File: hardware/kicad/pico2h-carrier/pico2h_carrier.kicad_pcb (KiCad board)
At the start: 2 copper layers, 92 x 82 mm, 0 parts

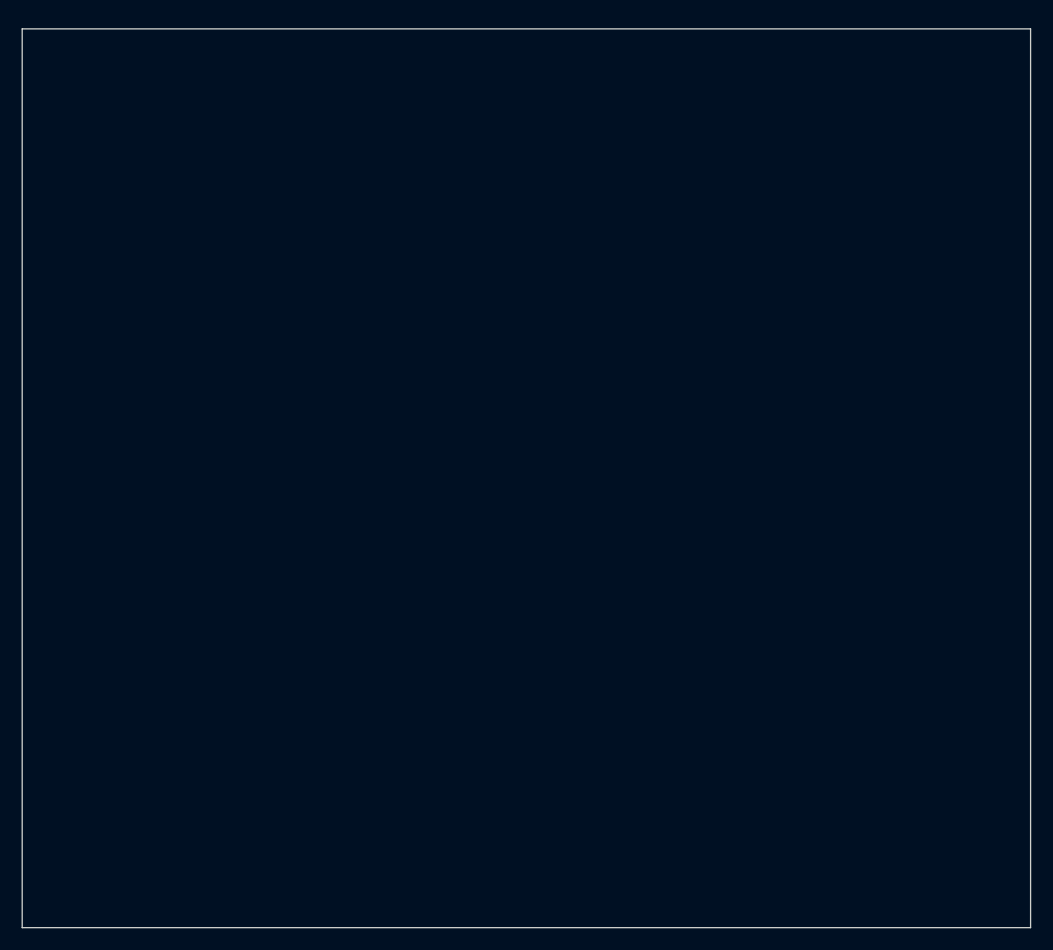
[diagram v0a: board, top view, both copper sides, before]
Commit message: feat: Pico 2 Hケースを58x38 mm基板・背面カメラのRev Cへ変更
基板を小さくし、カメラを背面へ移したうえで、印刷できる区切りの形状を残すため。
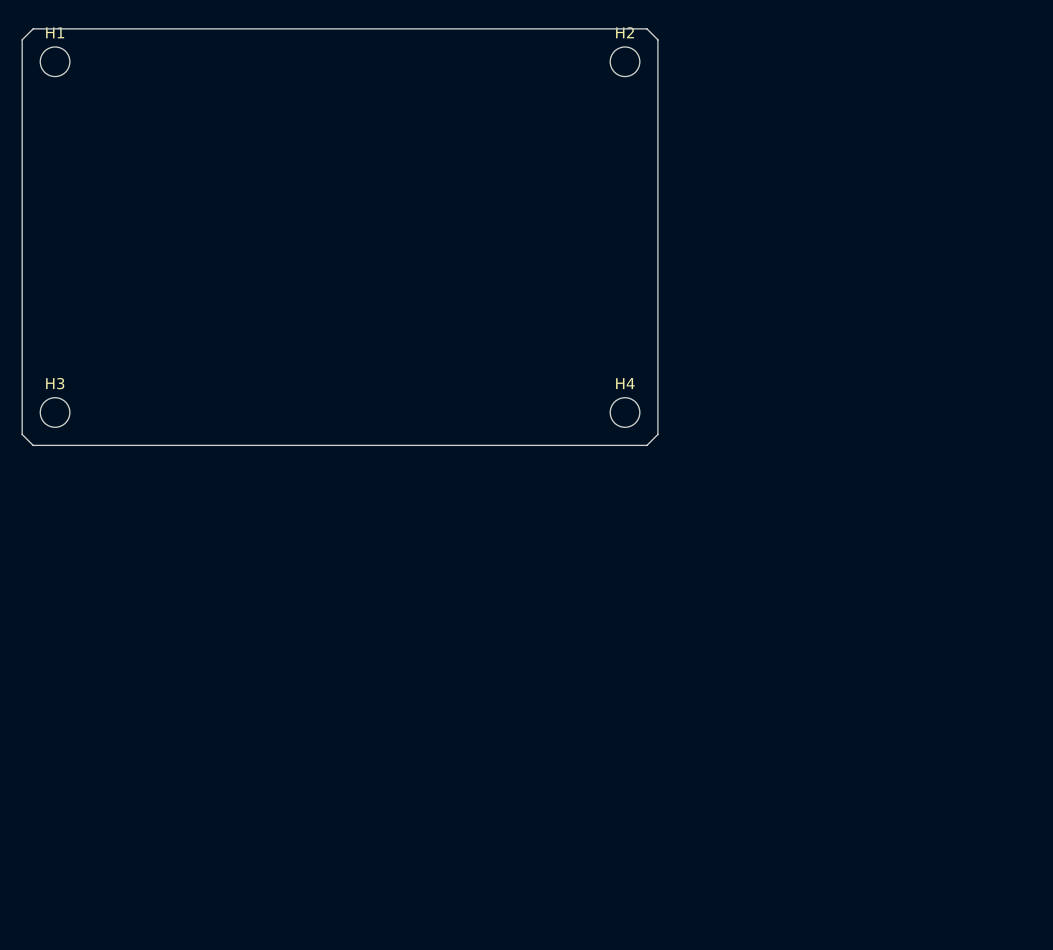
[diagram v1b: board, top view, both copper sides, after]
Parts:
- added H1: MountingHole_2.7mm_M2.5, MountingHole:MountingHole_2.7mm_M2.5, F.Cu at (3.00, 3.00)
- added H2: MountingHole_2.7mm_M2.5, MountingHole:MountingHole_2.7mm_M2.5, F.Cu at (55.0, 3.00)
- added H3: MountingHole_2.7mm_M2.5, MountingHole:MountingHole_2.7mm_M2.5, F.Cu at (3.00, 35.0)
- added H4: MountingHole_2.7mm_M2.5, MountingHole:MountingHole_2.7mm_M2.5, F.Cu at (55.0, 35.0)
- added MECH_CASE: , PicoCarrier:case_reference, F.Cu at (0.00, 0.00)
- added MECH_COMPONENTS: , PicoCarrier:components_reference, F.Cu at (0.00, 0.00)
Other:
- board size 92 x 82 mm -> 58 x 38 mm
- board text added: "B0070: rear-case-mounted"
- board text added: "J3 LCD harness (FRONT)"
- board text added: "J4 CAM harness (BACK)"
- board text added: "J5 UART (FRONT)"
- board text added: "LCD: cover-mounted"
- board text added: "Pico 2 H: BACK / USB left"
- board text added: "REV C MECHANICAL DRAFT - ELECTRICAL FOOTPRINTS / ROUTING PENDING"
- board text added: "SW1 (FRONT)"
- board text added: "SW2 (FRONT)"
- board text removed: "APPROVE"
- board text removed: "Camera B0070 30.5 x 30.5"
- board text removed: "FRONT: LCD + camera | REAR: Pico 2 H"
- board text removed: "LCD module 43.72 x 32"
- board text removed: "NEXT"
- board text removed: "Pico 2 H rear side 51 x 21; USB exits left"
- board text removed: "REV A - ENVELOPE ONLY; connector positions, mounting holes and routing are provisional"
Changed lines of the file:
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@@
   (setup (pad_to_mask_clearance 0))
   (net 0 "")
-  (gr_line (start 0 0) (end 92 0) (stroke (width 0.05) (type default)) (layer "Edge.Cuts"))
-  (gr_line (start 92 0) (end 92 82) (stroke (width 0.05) (type default)) (layer "Edge.Cuts"))
-  (gr_line (start 92 82) (end 0 82) (stroke (width 0.05) (type default)) (layer "Edge.Cuts"))
-  (gr_line (start 0 82) (end 0 0) (stroke (width 0.05) (type default)) (layer "Edge.Cuts"))
-  (gr_rect (start 4 4) (end 47.72 36) (stroke (width 0.12) (type default)) (fill (type none)) (layer "Dwgs.User"))
-  (gr_text "LCD module 43.72 x 32" (at 25.86 20 0) (layer "Dwgs.User") (effects (font (size 1.2 1.2) (thickness 0.18)) (justify center)))
-  (gr_rect (start 55.5 4.5) (end 86 35) (stroke (width 0.12) (type default)) (fill (type none)) (layer "Dwgs.User"))
-  (gr_text "Camera B0070 30.5 x 30.5" (at 70.75 20 0) (layer "Dwgs.User") (effects (font (size 1.2 1.2) (thickness 0.18)) (justify center)))
-  (gr_rect (start 20.5 54) (end 71.5 75) (stroke (width 0.12) (type default)) (fill (type none)) (layer "Dwgs.User"))
-  (gr_text "Pico 2 H rear side 51 x 21; USB exits left" (at 46 64.5 0) (layer "Dwgs.User") (effects (font (size 1.2 1.2) (thickness 0.18)) (justify center)))
-  (gr_rect (start 13 41) (end 19 47) (stroke (width 0.12) (type default)) (fill (type none)) (layer "Dwgs.User"))
-  (gr_text "NEXT" (at 16 49 0) (layer "Dwgs.User") (effects (font (size 1.2 1.2) (thickness 0.18)) (justify center)))
-  (gr_rect (start 31 41) (end 37 47) (stroke (width 0.12) (type default)) (fill (type none)) (layer "Dwgs.User"))
-  (gr_text "APPROVE" (at 34 49 0) (layer "Dwgs.User") (effects (font (size 1.2 1.2) (thickness 0.18)) (justify center)))
-  (gr_text "FRONT: LCD + camera | REAR: Pico 2 H" (at 46 51 0) (layer "Dwgs.User") (effects (font (size 1 1) (thickness 0.15)) (justify center)))
-  (gr_text "REV A - ENVELOPE ONLY; connector positions, mounting holes and routing are provisional" (at 46 80 0) (layer "Dwgs.User") (effects (font (size 1 1) (thickness 0.15)) (justify center)))
+  (gr_line (start 1 0) (end 57 0) (stroke (width 0.05) (type default)) (layer "Edge.Cuts"))
+  (gr_line (start 57 0) (end 58 1) (stroke (width 0.05) (type default)) (layer "Edge.Cuts"))
+  (gr_line (start 58 1) (end 58 37) (stroke (width 0.05) (type default)) (layer "Edge.Cuts"))
+  (gr_line (start 58 37) (end 57 38) (stroke (width 0.05) (type default)) (layer "Edge.Cuts"))
+  (gr_line (start 57 38) (end 1 38) (stroke (width 0.05) (type default)) (layer "Edge.Cuts"))
+  (gr_line (start 1 38) (end 0 37) (stroke (width 0.05) (type default)) (layer "Edge.Cuts"))
+  (gr_line (start 0 37) (end 0 1) (stroke (width 0.05) (type default)) (layer "Edge.Cuts"))
+  (gr_line (start 0 1) (end 1 0) (stroke (width 0.05) (type default)) (layer "Edge.Cuts"))
+  (footprint "MountingHole:MountingHole_2.7mm_M2.5" (layer "F.Cu") (at 3 3)
+          (attr board_only exclude_from_pos_files exclude_from_bom)
+          (fp_text reference "H1" (at 0 -2.6) (layer "F.SilkS") (effects (font (size 1 1) (thickness 0.15))))
+          (fp_text value "MountingHole_2.7mm_M2.5" (at 0 2.6) (layer "F.Fab") hide (effects (font (size 1 1) (thickness 0.15))))
+          (pad "" np_thru_hole circle (at 0 0) (size 2.7 2.7) (drill 2.7) (layers "*.Cu" "*.Mask")))
+  (footprint "MountingHole:MountingHole_2.7mm_M2.5" (layer "F.Cu") (at 55 3)
+          (attr board_only exclude_from_pos_files exclude_from_bom)
+          (fp_text reference "H2" (at 0 -2.6) (layer "F.SilkS") (effects (font (size 1 1) (thickness 0.15))))
+          (fp_text value "MountingHole_2.7mm_M2.5" (at 0 2.6) (layer "F.Fab") hide (effects (font (size 1 1) (thickness 0.15))))
+          (pad "" np_thru_hole circle (at 0 0) (size 2.7 2.7) (drill 2.7) (layers "*.Cu" "*.Mask")))
+  (footprint "MountingHole:MountingHole_2.7mm_M2.5" (layer "F.Cu") (at 3 35)
+          (attr board_only exclude_from_pos_files exclude_from_bom)
+          (fp_text reference "H3" (at 0 -2.6) (layer "F.SilkS") (effects (font (size 1 1) (thickness 0.15))))
+          (fp_text value "MountingHole_2.7mm_M2.5" (at 0 2.6) (layer "F.Fab") hide (effects (font (size 1 1) (thickness 0.15))))
+          (pad "" np_thru_hole circle (at 0 0) (size 2.7 2.7) (drill 2.7) (layers "*.Cu" "*.Mask")))
+  (footprint "MountingHole:MountingHole_2.7mm_M2.5" (layer "F.Cu") (at 55 35)
+          (attr board_only exclude_from_pos_files exclude_from_bom)
+          (fp_text reference "H4" (at 0 -2.6) (layer "F.SilkS") (effects (font (size 1 1) (thickness 0.15))))
+          (fp_text value "MountingHole_2.7mm_M2.5" (at 0 2.6) (layer "F.Fab") hide (effects (font (size 1 1) (thickness 0.15))))
+          (pad "" np_thru_hole circle (at 0 0) (size 2.7 2.7) (drill 2.7) (layers "*.Cu" "*.Mask")))
+  (gr_rect (start 7 3) (end 50.72 35) (stroke (width 0.12) (type default)) (fill (type none)) (layer "Dwgs.User"))
+  (gr_text "LCD: cover-mounted" (at 28.86 2) (layer "Dwgs.User") (effects (font (size 0.8 0.8) (thickness 0.12))))
+  (gr_rect (start 10 4) (end 40.5 34.5) (stroke (width 0.12) (type default)) (fill (type none)) (layer "Dwgs.User"))
+  (gr_text "B0070: rear-case-mounted" (at 25.25 3) (layer "Dwgs.User") (effects (font (size 0.8 0.8) (thickness 0.12))))
+  (gr_rect (start 2.5 8.5) (end 53.5 29.5) (stroke (width 0.12) (type default)) (fill (type none)) (layer "Dwgs.User"))
+  (gr_text "Pico 2 H: BACK / USB left" (at 28 7.5) (layer "Dwgs.User") (effects (font (size 0.8 0.8) (thickness 0.12))))
+  (gr_rect (start 12.5 8) (end 15 28.32) (stroke (width 0.12) (type default)) (fill (type none)) (layer "Dwgs.User"))
+  (gr_text "J3 LCD harness (FRONT)" (at 13.75 7) (layer "Dwgs.User") (effects (font (size 0.8 0.8) (thickness 0.12))))
+  (gr_rect (start 17.5 8) (end 20 13.08) (stroke (width 0.12) (type default)) (fill (type none)) (layer "Dwgs.User"))
+  (gr_text "J5 UART (FRONT)" (at 18.75 7) (layer "Dwgs.User") (effects (font (size 0.8 0.8) (thickness 0.12))))
+  (gr_rect (start 14 1.5) (end 39.4 6.58) (stroke (width 0.12) (type default)) (fill (type none)) (layer "Dwgs.User"))
+  (gr_text "J4 CAM harness (BACK)" (at 26.7 0.5) (layer "Dwgs.User") (effects (font (size 0.8 0.8) (thickness 0.12))))
+  (gr_rect (start 50.8 9) (end 56.8 15) (stroke (width 0.12) (type default)) (fill (type none)) (layer "Dwgs.User"))
+  (gr_text "SW1 (FRONT)" (at 53.8 8) (layer "Dwgs.User") (effects (font (size 0.8 0.8) (thickness 0.12))))
+  (gr_rect (start 50.8 23) (end 56.8 29) (stroke (width 0.12) (type default)) (fill (type none)) (layer "Dwgs.User"))
+  (gr_text "SW2 (FRONT)" (at 53.8 22) (layer "Dwgs.User") (effects (font (size 0.8 0.8) (thickness 0.12))))
+  (footprint "PicoCarrier:case_reference" (layer "F.Cu") (at 0 0)
+          (attr board_only exclude_from_pos_files exclude_from_bom)
+          (fp_text reference "MECH_CASE" (at 0 -5) (layer "F.Fab") hide (effects (font (size 1 1) (thickness 0.15))))
+          (model "${KIPRJMOD}/3dprint/case.wrl" (offset (xyz 0 0 0)) (scale (xyz 1 1 1)) (rotate (xyz 0 0 0))))
+  (footprint "PicoCarrier:components_reference" (layer "F.Cu") (at 0 0)
+          (attr board_only exclude_from_pos_files exclude_from_bom)
+          (fp_text reference "MECH_COMPONENTS" (at 0 -5) (layer "F.Fab") hide (effects (font (size 1 1) (thickness 0.15))))
+          (model "${KIPRJMOD}/3dprint/components.wrl" (offset (xyz 0 0 0)) (scale (xyz 1 1 1)) (rotate (xyz 0 0 0))))
+  (gr_text "REV C MECHANICAL DRAFT - ELECTRICAL FOOTPRINTS / ROUTING PENDING" (at 29 41) (layer "Dwgs.User") (effects (font (size 0.9 0.9) (thickness 0.12))))
 )
